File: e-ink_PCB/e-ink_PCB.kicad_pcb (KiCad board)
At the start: 2 copper layers, 70 x 35 mm, 10 parts, among them J1 SEEED C3, J2 "Dreams and Gasoline", J3 SHT31, J4 C2, J5 Battery, Q1 FQP27P06

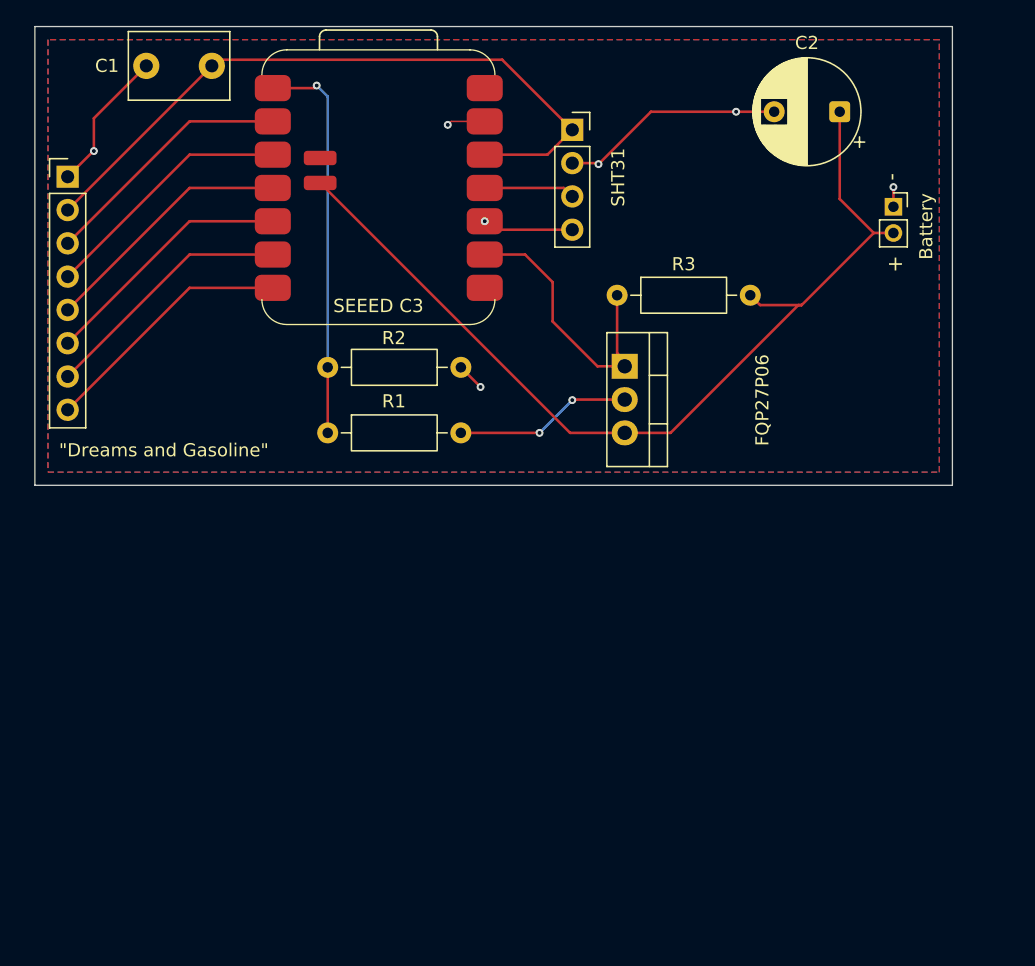
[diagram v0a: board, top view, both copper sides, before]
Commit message: kiCAD correct display orientation
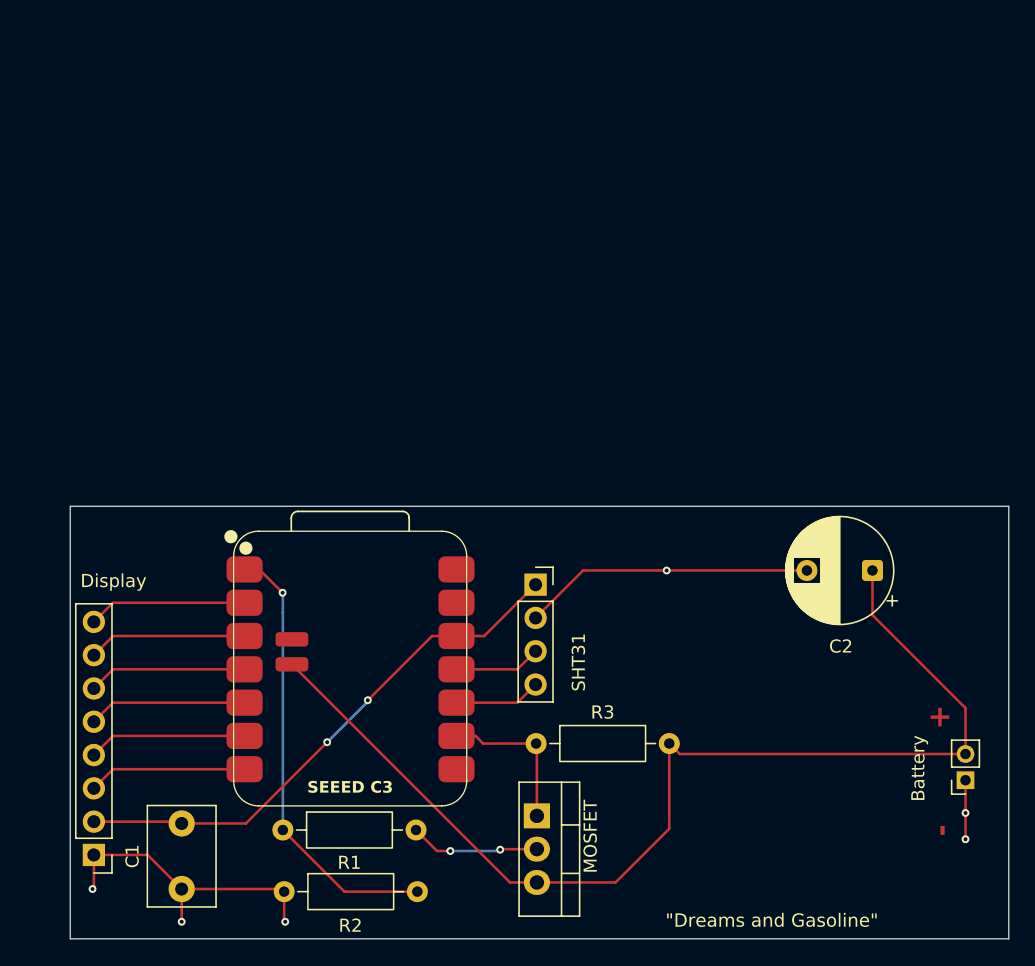
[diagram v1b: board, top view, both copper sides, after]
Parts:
- removed J2: "Dreams and Gasoline", Connector_PinHeader_2.54mm:PinHeader_1x08_P2.54mm_Vertical
- removed Q1: FQP27P06, Package_TO_SOT_THT:TO-220-3_Vertical
- added Display: e-ink-display, Connector_PinHeader_2.54mm:PinHeader_1x08_P2.54mm_Vertical, F.Cu at (76.5, 118.2)
- added MOSFET: FQP27P06, Package_TO_SOT_THT:TO-220-3_Vertical, F.Cu at (110.3, 115.2)
- moved C1 62.9 mm to (83.2, 120.8), turned to 90 degrees
- moved J5 44.1 mm to (143.0, 112.5), turned to 180 degrees
- moved R2 42.2 mm to (91.0, 121.0), turned to 0 degrees
- moved J1 36.8 mm to (96.0, 104.0)
- moved J4 35.1 mm to (135.9, 96.5)
- moved J3 34.8 mm to (110.2, 97.6)
- moved R3 34.8 mm to (110.2, 109.7)
- moved R1 30.5 mm to (90.9, 116.3)
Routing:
- net GND: track 34.6 -> 49.9 mm
- net Net-(J4-Pin_2): track 72.5 -> 83.8 mm
- net Net-(J2-Pin_2): track 52.3 -> 41.4 mm, vias 0 -> 2
- net Net-(Q1-G): track 21.6 -> 11.9 mm
- net Net-(J2-Pin_7): track 19.5 -> 12.1 mm
- net Net-(J2-Pin_6): track 19.5 -> 12.1 mm
- net Net-(J2-Pin_4): track 19.5 -> 12.1 mm
- net Net-(J2-Pin_8): track 19.5 -> 12.1 mm
- net Net-(J2-Pin_5): track 19.5 -> 12.1 mm
- net Net-(J2-Pin_3): track 19.5 -> 12.1 mm
- net Net-(J1-Pin_8): track 30.3 -> 34.0 mm
- net Net-(Q1-D): track 13.6 -> 9.94 mm
- net Net-(J3-Pin_4): track 6.95 -> 6.61 mm, vias 1 -> 0
- removed copper zone on B.Cu, net GND
- removed copper zone on F.Cu, net GND
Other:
- board size 70 x 35 mm -> 71.6 x 33 mm
- board text added: "{dblquote}Dreams and Gasoline{dblquote}"
